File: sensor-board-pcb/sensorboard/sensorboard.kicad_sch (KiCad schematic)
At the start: 19 parts, among them J1 TO_MOTHERBOARD, J10 PZT_08, J11 PZT_09, J12 PZT_10, J13 PZT_11, J14 PZT_12, J15 PZT_13, J16 PZT_14, J17 PZT_15, J2 PZT_00, J3 PZT_01, J4 PZT_02, J5 PZT_03, J6 PZT_04, J7 PZT_05, J8 PZT_06, J9 PZT_07, U1 CD74HC4067M

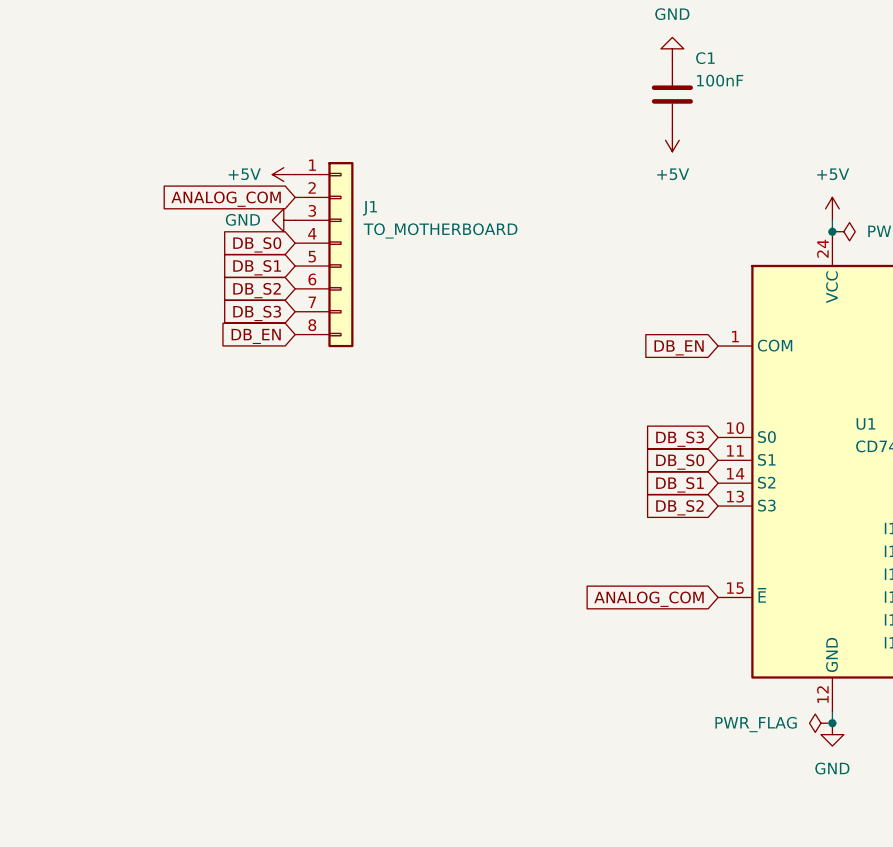
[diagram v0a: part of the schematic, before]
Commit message: fixed schematic and finished routing
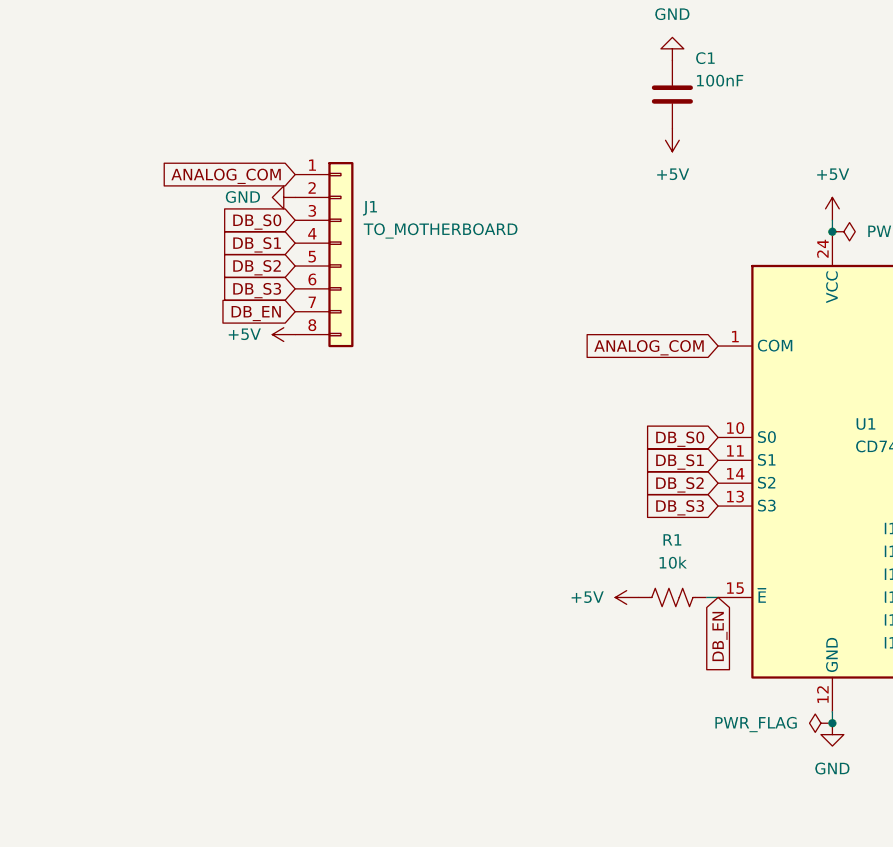
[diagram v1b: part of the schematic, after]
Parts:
- added R1: 10k, Resistor_THT:R_Axial_DIN0207_L6.3mm_D2.5mm_P7.62mm_Horizontal, symbol Device:R_US
- C1: footprint Capacitor_SMD:C_0603_1608Metric -> Capacitor_THT:C_Disc_D5.0mm_W2.5mm_P5.00mm
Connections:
- net +5V: now also J1.8 (Pin_8), R1.1; no longer J1.1 (Pin_1)
- net ANALOG_COM: now also J1.1 (Pin_1), U1.1 (COM); no longer J1.2 (Pin_2), U1.15 (~{E})
- net DB_EN: now also J1.7 (Pin_7), U1.15 (~{E}), R1.2; no longer J1.8 (Pin_8), U1.1 (COM)
- net DB_S0: now also J1.3 (Pin_3), U1.10 (S0); no longer J1.4 (Pin_4), U1.11 (S1)
- net DB_S1: now also J1.4 (Pin_4), U1.11 (S1); no longer J1.5 (Pin_5), U1.14 (S2)
- net DB_S2: now also J1.5 (Pin_5), U1.14 (S2); no longer J1.6 (Pin_6), U1.13 (S3)
- net DB_S3: now also J1.6 (Pin_6), U1.13 (S3); no longer J1.7 (Pin_7), U1.10 (S0)
- net GND: now also J1.2 (Pin_2); no longer J1.3 (Pin_3)
